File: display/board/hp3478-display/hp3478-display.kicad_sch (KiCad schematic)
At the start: 24 parts, among them J1 SFV10R-1ST, J2 DNP, U1 PIC16F15274-I/MP, U2 DNP

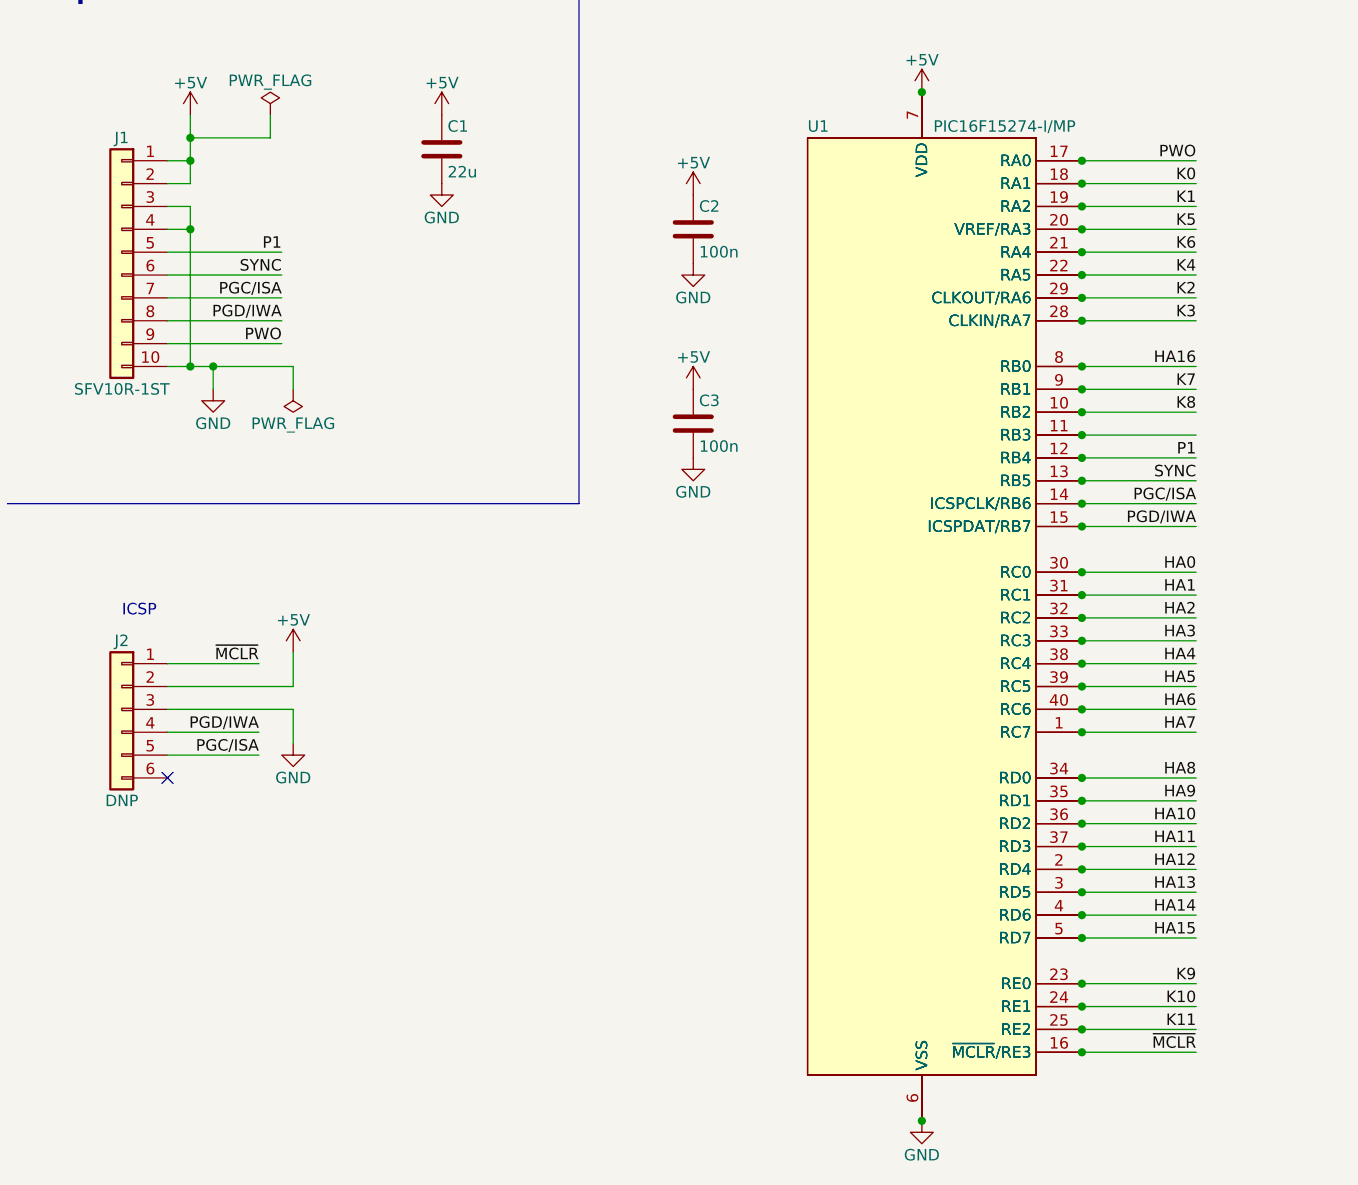
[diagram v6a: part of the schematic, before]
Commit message: Route LED cathode nets.
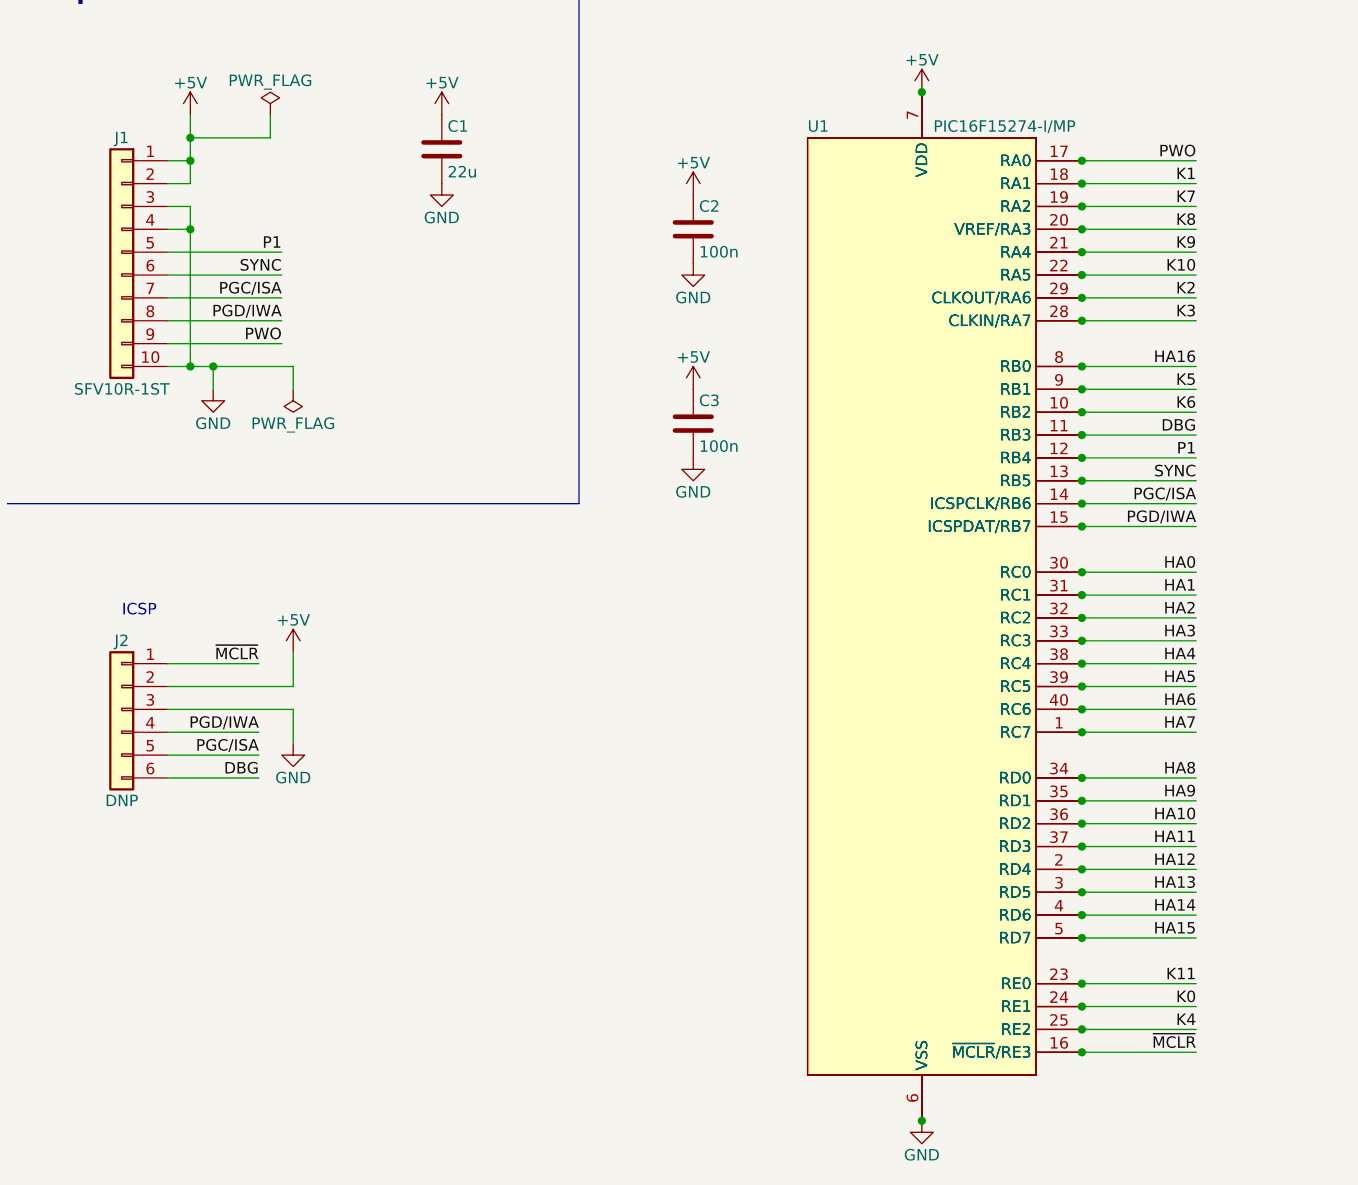
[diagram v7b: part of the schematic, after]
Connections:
- net K0: now also U1.24 (RE1), U2.26 (RE1); no longer U1.18 (RA1), U2.20 (RA1)
- net K1: now also U1.18 (RA1), U2.20 (RA1); no longer U1.19 (RA2), U2.21 (RA2)
- net K10: now also U1.22 (RA5), U2.24 (RA5); no longer U1.24 (RE1), U2.26 (RE1)
- net K11: now also U1.23 (RE0), U2.25 (RE0); no longer U1.25 (RE2), U2.27 (RE2)
- net K4: now also U1.25 (RE2), U2.27 (RE2); no longer U1.22 (RA5), U2.24 (RA5)
- net K5: now also U1.9 (RB1), U2.9 (RB1); no longer U1.20 (VREF/RA3), U2.22 (VREF/RA3)
- net K6: now also U1.10 (RB2), U2.10 (RB2); no longer U1.21 (RA4), U2.23 (RA4)
- net K7: now also U1.19 (RA2), U2.21 (RA2); no longer U1.9 (RB1), U2.9 (RB1)
- net K8: now also U1.20 (VREF/RA3), U2.22 (VREF/RA3); no longer U1.10 (RB2), U2.10 (RB2)
- net K9: now also U1.21 (RA4), U2.23 (RA4); no longer U1.23 (RE0), U2.25 (RE0)
- net DBG: now reaches U1.11 (RB3), U2.11 (RB3)
- net DBG: now also J2.6 (Pin_6)
- no-connect marks 1 -> 0
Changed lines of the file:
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@@
   (junction (at 132.08 93.98) (diameter 0) (color 0 0 0 0)
   )
-  (no_connect (at 30.48 157.48))
   (wire (pts (xy 187.96 58.42) (xy 198.12 58.42))
     (stroke (width 0) (type default) (color 0 0 0 0))
@@
   )
   (wire (pts (xy 210.82 106.68) (xy 226.06 106.68))
+    (stroke (width 0) (type default) (color 0 0 0 0))
+  )
+  (wire (pts (xy 30.48 157.48) (xy 40.64 157.48))
     (stroke (width 0) (type default) (color 0 0 0 0))
   )
@@
     (effects (font (size 3.81 3.81)) (justify left bottom))
   )
-  (label "K6" (at 144.78 99.06 180)
+  (label "K6" (at 144.78 116.84 180)
     (effects (font (size 1.27 1.27)) (justify right bottom))
   )
@@
     (effects (font (size 1.27 1.27)) (justify left bottom))
   )
+  (label "DBG" (at 144.78 119.38 180)
+    (effects (font (size 1.27 1.27)) (justify right bottom))
+  )
   (label "SYNC" (at 144.78 124.46 180)
     (effects (font (size 1.27 1.27)) (justify right bottom))
@@
     (effects (font (size 1.27 1.27)) (justify left bottom))
   )
-  (label "K1" (at 144.78 93.98 180)
+  (label "K1" (at 144.78 91.44 180)
     (effects (font (size 1.27 1.27)) (justify right bottom))
   )
@@
     (effects (font (size 1.27 1.27)) (justify right bottom))
   )
-  (label "K10" (at 144.78 182.88 180)
+  (label "K10" (at 144.78 101.6 180)
     (effects (font (size 1.27 1.27)) (justify right bottom))
   )
@@
     (effects (font (size 1.27 1.27)) (justify left bottom))
   )
-  (label "K5" (at 144.78 96.52 180)
+  (label "K5" (at 144.78 114.3 180)
     (effects (font (size 1.27 1.27)) (justify right bottom))
   )
@@
     (effects (font (size 1.27 1.27)) (justify left bottom))
   )
-  (label "K0" (at 144.78 91.44 180)
+  (label "K0" (at 144.78 182.88 180)
     (effects (font (size 1.27 1.27)) (justify right bottom))
   )
@@
     (effects (font (size 1.27 1.27)) (justify left bottom))
   )
-  (label "K8" (at 144.78 116.84 180)
+  (label "K8" (at 144.78 96.52 180)
     (effects (font (size 1.27 1.27)) (justify right bottom))
   )
@@
     (effects (font (size 1.27 1.27)) (justify right bottom))
   )
-  (label "K4" (at 144.78 101.6 180)
+  (label "K4" (at 144.78 185.42 180)
     (effects (font (size 1.27 1.27)) (justify right bottom))
   )
@@
     (effects (font (size 1.27 1.27)) (justify right bottom))
   )
+  (label "DBG" (at 40.64 157.48 180)
+    (effects (font (size 1.27 1.27)) (justify right bottom))
+  )
   (label "HA14" (at 144.78 172.72 180)
     (effects (font (size 1.27 1.27)) (justify right bottom))
@@
     (effects (font (size 1.27 1.27)) (justify right bottom))
   )
-  (label "K7" (at 144.78 114.3 180)
+  (label "K7" (at 144.78 93.98 180)
     (effects (font (size 1.27 1.27)) (justify right bottom))
   )
@@
     (effects (font (size 1.27 1.27)) (justify right bottom))
   )
-  (label "K11" (at 144.78 185.42 180)
-    (effects (font (size 1.27 1.27)) (justify right bottom))
-  )
-  (label "K9" (at 144.78 180.34 180)
-    (effects (font (size 1.27 1.27)) (justify right bottom))
-  )
+  (label "K11" (at 144.78 180.34 180)
+    (effects (font (size 1.27 1.27)) (justify right bottom))
+  )
+  (label "K9" (at 144.78 99.06 180)
+    (effects (font (size 1.27 1.27)) (justify right bottom))
+  )

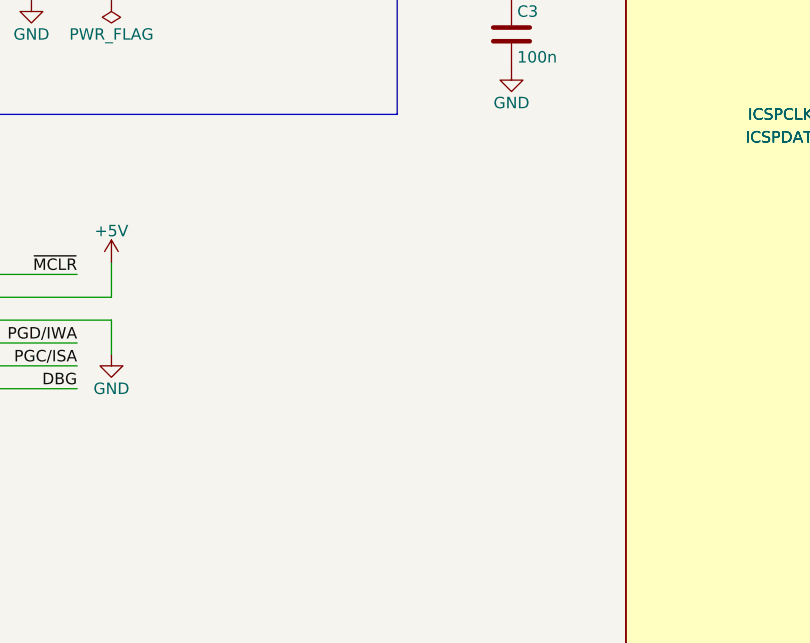
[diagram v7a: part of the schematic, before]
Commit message: Route inputs and MCU support nets.
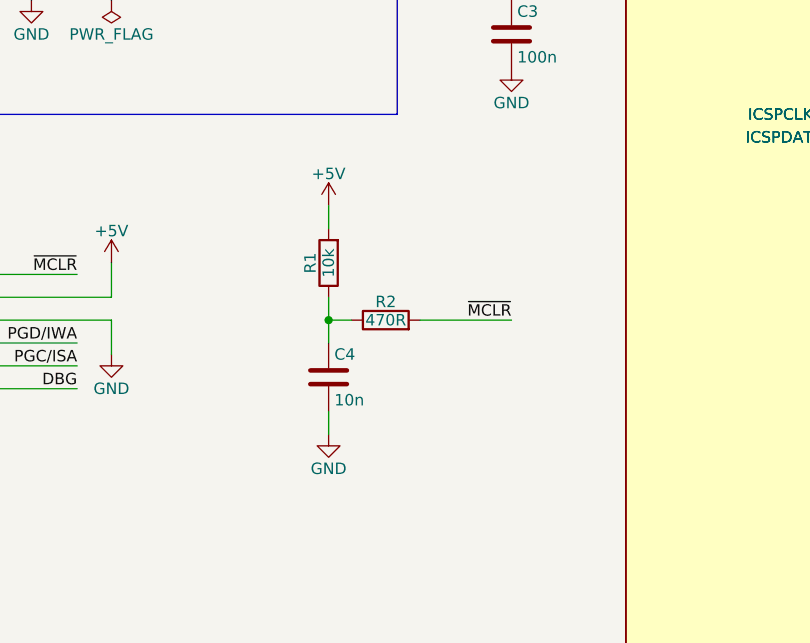
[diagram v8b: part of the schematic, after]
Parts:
- added C4: 10n, Capacitor_SMD:C_0603_1608Metric, symbol Device:C
- added R1: 10k, Resistor_SMD:R_0603_1608Metric, symbol Device:R
- added R2: 470R, Resistor_SMD:R_0603_1608Metric, symbol Device:R
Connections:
- net +5V: now also R1.2
- net GND: now also C4.2
- net ~{MCLR}: now also R2.2
- new net: C4.1, R1.1, R2.1
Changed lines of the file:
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@@
   (junction (at 132.08 157.48) (diameter 0) (color 0 0 0 0)
   )
+  (junction (at 68.58 149.86) (diameter 0) (color 0 0 0 0)
+  )
   (junction (at 132.08 180.34) (diameter 0) (color 0 0 0 0)
   )
@@
     (stroke (width 0) (type default) (color 0 0 0 0))
   )
+  (wire (pts (xy 68.58 147.32) (xy 68.58 149.86))
+    (stroke (width 0) (type default) (color 0 0 0 0))
+  )
+  (wire (pts (xy 68.58 137.16) (xy 68.58 139.7))
+    (stroke (width 0) (type default) (color 0 0 0 0))
+  )
   (wire (pts (xy 233.68 83.82) (xy 241.3 83.82))
     (stroke (width 0) (type default) (color 0 0 0 0))
@@
     (stroke (width 0) (type default) (color 0 0 0 0))
   )
+  (wire (pts (xy 68.58 149.86) (xy 68.58 152.4))
+    (stroke (width 0) (type default) (color 0 0 0 0))
+  )
   (wire (pts (xy 233.68 93.98) (xy 241.3 93.98))
     (stroke (width 0) (type default) (color 0 0 0 0))
@@
     (stroke (width 0) (type default) (color 0 0 0 0))
   )
+  (wire (pts (xy 68.58 149.86) (xy 71.12 149.86))
+    (stroke (width 0) (type default) (color 0 0 0 0))
+  )
   (wire (pts (xy 238.76 53.34) (xy 238.76 58.42))
+    (stroke (width 0) (type default) (color 0 0 0 0))
+  )
+  (wire (pts (xy 68.58 160.02) (xy 68.58 162.56))
+    (stroke (width 0) (type default) (color 0 0 0 0))
+  )
+  (wire (pts (xy 78.74 149.86) (xy 88.9 149.86))
     (stroke (width 0) (type default) (color 0 0 0 0))
   )
@@
   (label "K8" (at 187.96 58.42 0)
     (effects (font (size 1.27 1.27)) (justify left bottom))
+  )
+  (label "~{MCLR}" (at 88.9 149.86 180)
+    (effects (font (size 1.27 1.27)) (justify right bottom))
   )
   (label "A15" (at 241.3 124.46 180)
@@
     )
     (property "Datasheet" "" (id 3) (at 88.9 92.71 0)
+      (effects (font (size 1.27 1.27)) hide)
+    )
+    (pin "1")
+  )
+  (symbol (lib_id "power:GND") (at 68.58 162.56 0) (unit 1)
+    (in_bom yes) (on_board yes)
+    (property "Reference" "#PWR08" (id 0) (at 68.58 168.91 0)
+      (effects (font (size 1.27 1.27)) hide)
+    )
+    (property "Value" "GND" (id 1) (at 68.58 166.37 0))
+    (property "Footprint" "" (id 2) (at 68.58 162.56 0)
+      (effects (font (size 1.27 1.27)) hide)
+    )
+    (property "Datasheet" "" (id 3) (at 68.58 162.56 0)
       (effects (font (size 1.27 1.27)) hide)
     )
@@
     (pin "1")
   )
+  (symbol (lib_id "Device:R") (at 68.58 143.51 180) (unit 1)
+    (in_bom yes) (on_board yes)
+    (property "Reference" "R1" (id 0) (at 66.548 143.51 90))
+    (property "Value" "10k" (id 1) (at 68.58 143.51 90))
+    (property "Footprint" "Resistor_SMD:R_0603_1608Metric" (id 2) (at 70.358 143.51 90)
+      (effects (font (size 1.27 1.27)) hide)
+    )
+    (property "Datasheet" "~" (id 3) (at 68.58 143.51 0)
+      (effects (font (size 1.27 1.27)) hide)
+    )
+    (pin "1")
+    (pin "2")
+  )
   (symbol (lib_id "Device:R") (at 229.87 106.68 90) (unit 1)
     (in_bom yes) (on_board yes)
@@
     (pin "1")
     (pin "2")
+  )
+  (symbol (lib_id "power:+5V") (at 68.58 137.16 0) (mirror y) (unit 1)
+    (in_bom yes) (on_board yes)
+    (property "Reference" "#PWR07" (id 0) (at 68.58 140.97 0)
+      (effects (font (size 1.27 1.27)) hide)
+    )
+    (property "Value" "+5V" (id 1) (at 68.58 133.604 0))
+    (property "Footprint" "" (id 2) (at 68.58 137.16 0)
+      (effects (font (size 1.27 1.27)) hide)
+    )
+    (property "Datasheet" "" (id 3) (at 68.58 137.16 0)
+      (effects (font (size 1.27 1.27)) hide)
+    )
+    (pin "1")
   )
   (symbol (lib_name "Digit_Legend_5") (lib_id "0Local:Digit_Legend") (at 50.165 41.275 0) (unit 1)
@@
     (pin "2")
   )
+  (symbol (lib_id "Device:C") (at 68.58 156.21 0) (unit 1)
+    (in_bom yes) (on_board yes)
+    (property "Reference" "C4" (id 0) (at 69.215 153.67 0)
+      (effects (font (size 1.27 1.27)) (justify left))
+    )
+    (property "Value" "10n" (id 1) (at 69.215 158.75 0)
+      (effects (font (size 1.27 1.27)) (justify left))
+    )
+    (property "Footprint" "Capacitor_SMD:C_0603_1608Metric" (id 2) (at 69.5452 160.02 0)
+      (effects (font (size 1.27 1.27)) hide)
+    )
+    (property "Datasheet" "~" (id 3) (at 68.58 156.21 0)
+      (effects (font (size 1.27 1.27)) hide)
+    )
+    (pin "1")
+    (pin "2")
+  )
   (symbol (lib_name "Digit_Legend_3") (lib_id "0Local:Digit_Legend") (at 70.485 41.275 0) (unit 1)
     (in_bom no) (on_board no)
@@
     )
     (pin "1")
+  )
+  (symbol (lib_id "Device:R") (at 74.93 149.86 90) (unit 1)
+    (in_bom yes) (on_board yes)
+    (property "Reference" "R2" (id 0) (at 74.93 147.828 90))
+    (property "Value" "470R" (id 1) (at 74.93 149.86 90))
+    (property "Footprint" "Resistor_SMD:R_0603_1608Metric" (id 2) (at 74.93 151.638 90)
+      (effects (font (size 1.27 1.27)) hide)
+    )
+    (property "Datasheet" "~" (id 3) (at 74.93 149.86 0)
+      (effects (font (size 1.27 1.27)) hide)
+    )
+    (pin "1")
+    (pin "2")
   )
   (sheet (at 246.38 33.02) (size 13.97 20.32) (fields_autoplaced)
@@
       (reference "#PWR06") (unit 1) (value "GND") (footprint "")
     )
+    (path "/470b1047-dcdd-4693-af35-1e38a72d5443"
+      (reference "#PWR07") (unit 1) (value "+5V") (footprint "")
+    )
+    (path "/11c51e60-7c6c-4b40-80fd-5eb1ccc32582"
+      (reference "#PWR08") (unit 1) (value "GND") (footprint "")
+    )
     (path "/3b3d7e06-ee84-4259-83f3-df57614f4ff5"
       (reference "#PWR0101") (unit 1) (value "+5V") (footprint "")
@@
       (reference "C3") (unit 1) (value "100n") (footprint "Capacitor_SMD:C_0603_1608Metric")
     )
+    (path "/cbbcda82-8ebd-4c3a-a5d2-7f4cb411f167"
+      (reference "C4") (unit 1) (value "10n") (footprint "Capacitor_SMD:C_0603_1608Metric")
+    )
     (path "/a02a9f23-494b-4654-bad5-fd847fe0e184/926fffe8-740d-4331-ba23-3fdb7006389d"
       (reference "D201") (unit 1) (value "LED") (footprint "0Local:LED_0402_1005Metric")
@@
       (reference "J2") (unit 1) (value "DNP") (footprint "Connector_PinHeader_2.54mm:PinHeader_1x06_P2.54mm_Vertical")
     )
+    (path "/3cbbce61-b5d9-4674-95bd-40b1d2689517"
+      (reference "R1") (unit 1) (value "10k") (footprint "Resistor_SMD:R_0603_1608Metric")
+    )
+    (path "/f9510427-fa72-4f90-8f57-032ea1ed7cd0"
+      (reference "R2") (unit 1) (value "470R") (footprint "Resistor_SMD:R_0603_1608Metric")
+    )
     (path "/b9ac1e92-9153-475c-aa48-df2e77e44760"
